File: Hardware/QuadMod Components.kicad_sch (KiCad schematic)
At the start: 119 parts, among them J1 Conn_01x08_Pin, J2 Conn_01x08_Pin, J3 Conn_01x08_Pin, J4 Conn_01x08_Pin, J5 Eurorack_10_pin_power, J7 Prog_Header, J7 USB_B_Micro, J8 Extra_Outs, U1 STF202-22T1G, U2 STM32H563VIT, U3 TL072, U4 MCP6004, U6 TPS561201, U7 LD1117-3.3-4Tab, U7 MCP6002-xSN, U9 AK4619VN, Y1 8MHz 20pF

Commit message: Clean up of schematics and PCBS
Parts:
- added J9: Test_Outs, Connector_PinHeader_2.54mm:PinHeader_1x02_P2.54mm_Vertical, symbol Connector:Conn_01x02_Pin
- added TP9: TestPoint, Custom_Footprints:1mm_Test_Point, symbol Connector:TestPoint
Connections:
- net +3.3VA: now also J4.4 (Pin_4); no longer J4.3 (Pin_3)
- net DLY_MIX: now also J4.3 (Pin_3); no longer J4.2 (Pin_2)
- net FX_MIX: now also J4.5 (Pin_5); no longer J4.4 (Pin_4)
- net GND: now also J4.1 (Pin_1), TP9.1; no longer J4.7 (Pin_7)
- net LFO_RANGE: now also J4.2 (Pin_2); no longer J4.1 (Pin_1)
- net OUT_AMP1: now also J4.7 (Pin_7); no longer J4.6 (Pin_6)
- net OUT_AMP2: now also J4.6 (Pin_6); no longer J4.5 (Pin_5)
- net Test_Out1: now reaches U2.78 (PC10)
- net Test_Out1: now also J9.1 (Pin_1)
- net Test_Out2: now reaches U2.79 (PC11)
- net Test_Out2: now also J9.2 (Pin_2)
- no-connect marks 50 -> 49
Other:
- note added: "(-5*-47/75) + (cv*-47/91) + (pot*-47/47) Pot=0 CV=0: 3.13V Pot=0 CV=6: 0.034V Pot=3.3 CV=0: -0.17V Pot=3.3 CV=5: -2.75V"
- note added: "Audio Codec"
- note added: "Av = -R_{FB} / R_{IN} Input: +7V, Output: (-12 * -14k/100k) + (+7 * -14k/68k) = 0.24V Input: -7V Output: (-12 * -14k/100k) + (-7 * -14k/68k) = 3.12V"
- note added: "Connectors"
- note added: "DAC Output is 2.83V_{PP} 10k/14k gives gain of 2.4 * 2.83 = 6.8V HPF Cutoff = 0.41Hz"
- note added: "MCU"
- note added: "USB"
- note removed: "Audio DAC"
- note removed: "Av = -R_{FB} / R_{IN} Input: +7V, Output: (-12 * -14k/100k) + (+7 * 14k/68k) = 0.24V Input: -7V Output: (-12 * -14k/100k) + (-7 * 14k/68k) = 3.12V"
- note removed: "DAC Output is 2.83V_{PP} 10k/14k gives gain of 2.4 * 2.83 = 6.8V"
- note removed: "POT Full scale: 3.3V CV Full scale: 6.4V"
- company: (none) -> Mountjoy Modular
- title: (none) -> QuadMod Components
- moved on the sheet: C12, C13, C18, C19, C38, C39, C40, C41, C42, C43, C44, D1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

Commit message: Draft Gerber Creation
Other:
- moved on the sheet: R10, R11, R12, R13, R14, R15, R16, R17, R6, R7, R8, R9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

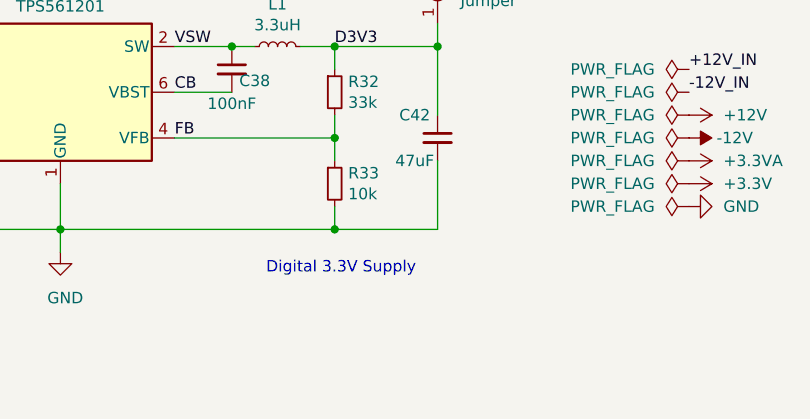
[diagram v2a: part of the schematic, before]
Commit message: Updated Production Gerbers; attempts to get USB working with O1 optimisation
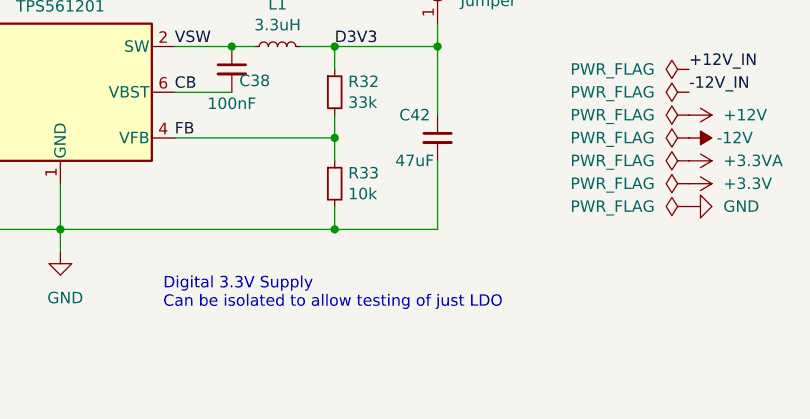
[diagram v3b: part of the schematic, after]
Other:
- note added: "Digital 3.3V Supply Can be isolated to allow testing of just LDO"
- note removed: "Digital 3.3V Supply"
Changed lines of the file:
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@@
     (effects (font (size 3 3) (thickness 0.6) bold) (justify left bottom))
   )
-  (text "Digital 3.3V Supply" (at 125.73 270.51 0)
+  (text "Digital 3.3V Supply\nCan be isolated to allow testing of just LDO"
+    (at 114.3 274.32 0)
     (effects (font (size 1.27 1.27)) (justify left bottom))
   )

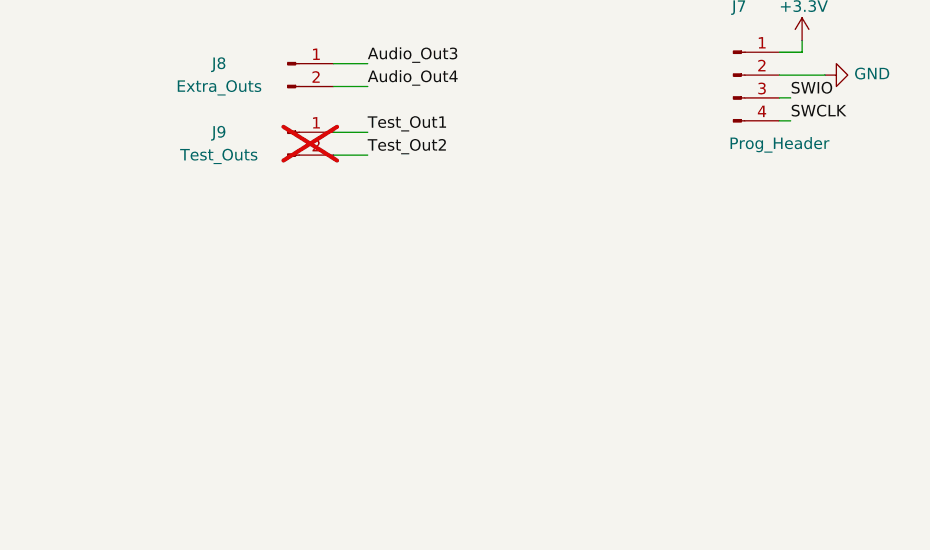
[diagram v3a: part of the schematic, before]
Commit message: Audio codec output tested and working
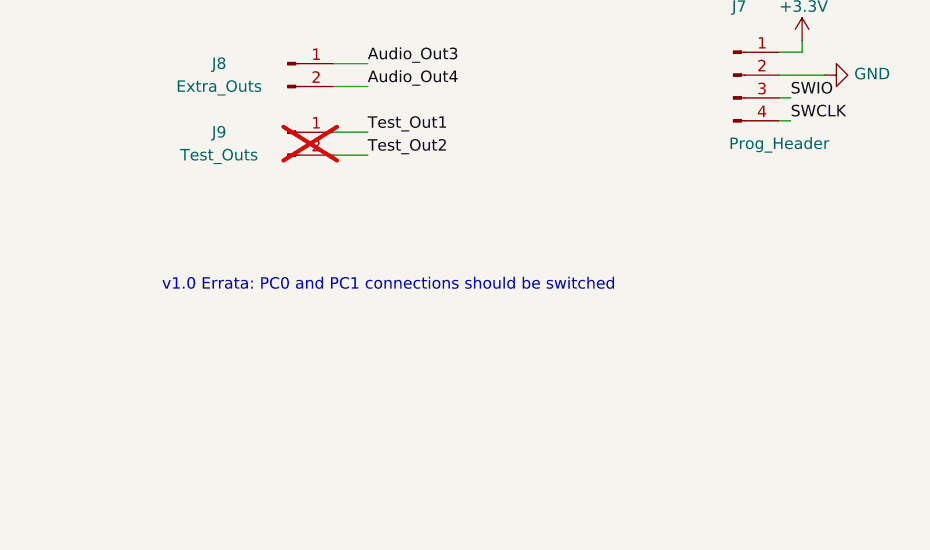
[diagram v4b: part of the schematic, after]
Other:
- note added: "v1.0 Errata: PC0 and PC1 connections should be switched"
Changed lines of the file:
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@@
+    (effects (font (size 1.27 1.27)) (justify left bottom))
+  )
+  (text "v1.0 Errata: PC0 and PC1 connections should be switched"
+    (at 303.53 257.81 0)
     (effects (font (size 1.27 1.27)) (justify left bottom))
   )

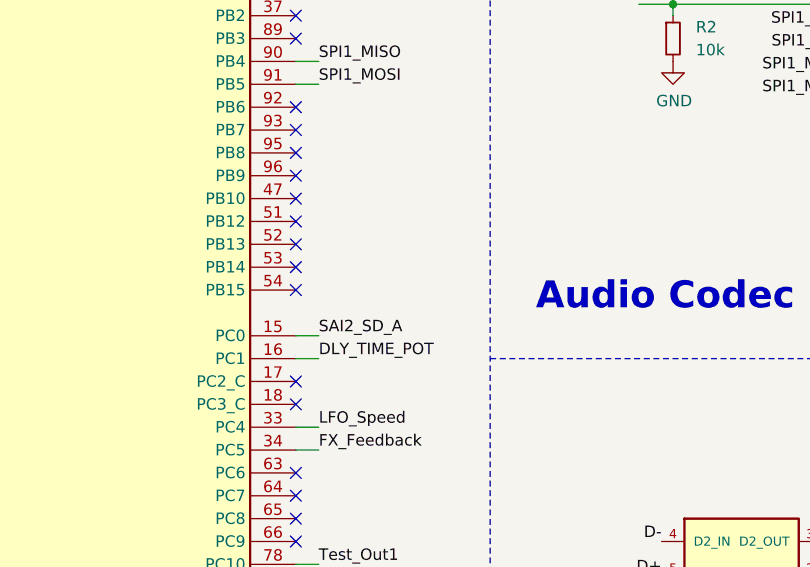
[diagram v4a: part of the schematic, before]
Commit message: Updated GpioPIn.h; basic delay LED working
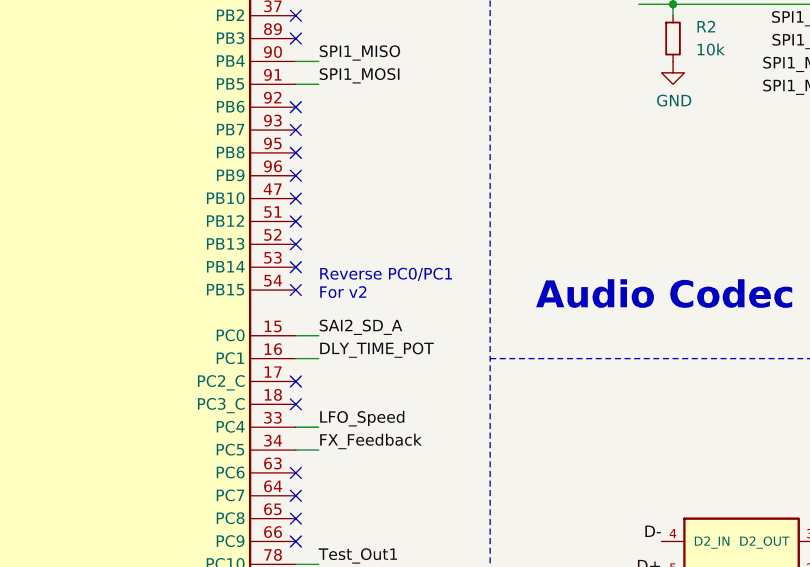
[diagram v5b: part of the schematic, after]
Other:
- note added: "Reverse PC0/PC1 For v2"
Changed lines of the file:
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@@
     (effects (font (size 1.27 1.27)) (justify left bottom))
+  )
+  (text "Reverse PC0/PC1 \nFor v2" (at 85.09 128.27 0)
+    (effects (font (size 1.27 1.27) (color 255 0 0 1)) (justify left bottom))
   )
   (text "USB" (at 109.22 189.23 0)
@@
   )
   (label "DLY_TIME_POT" (at 85.09 134.62 0) (fields_autoplaced)
-    (effects (font (size 1.27 1.27)) (justify left bottom))
+    (effects (font (size 1.27 1.27) (color 255 0 0 1)) (justify left bottom))
   )
   (label "SPI1_SCK" (at 85.09 60.96 0) (fields_autoplaced)
@@
   )
   (label "SAI2_SD_A" (at 85.09 132.08 0) (fields_autoplaced)
-    (effects (font (size 1.27 1.27)) (justify left bottom))
+    (effects (font (size 1.27 1.27) (color 255 0 0 1)) (justify left bottom))
   )
   (label "LFO_SPEED_POT" (at 250.19 217.17 0) (fields_autoplaced)

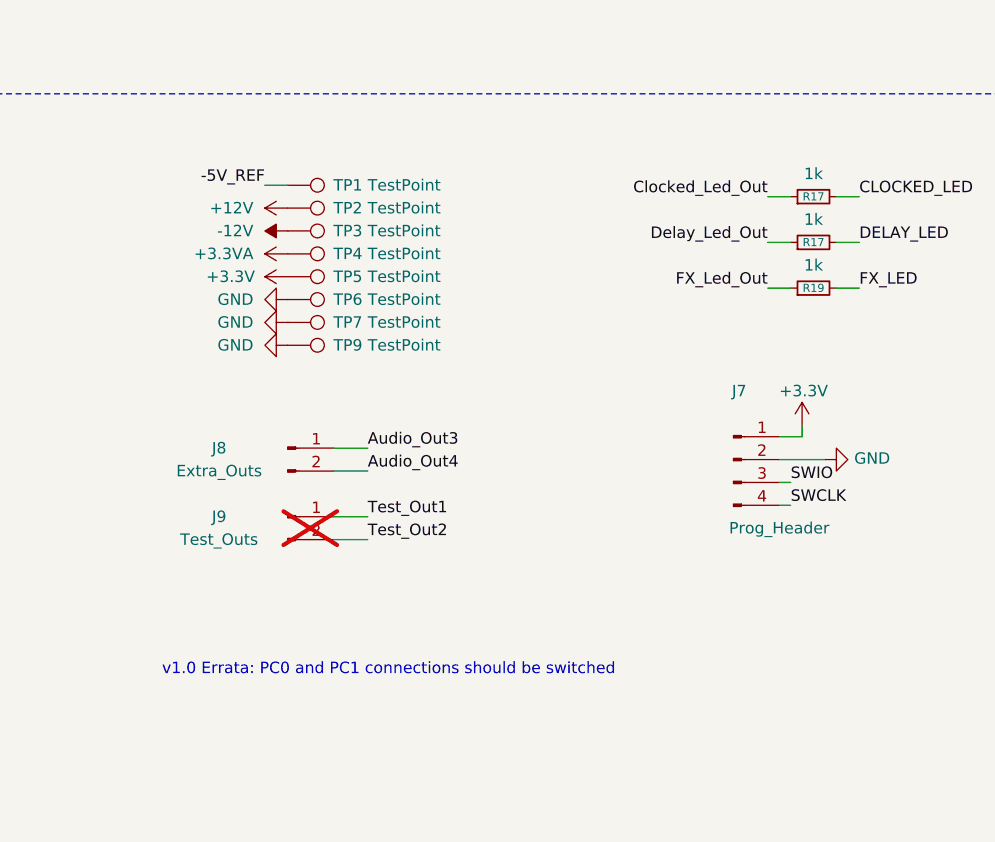
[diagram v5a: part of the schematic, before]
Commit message: Implemented effect switching
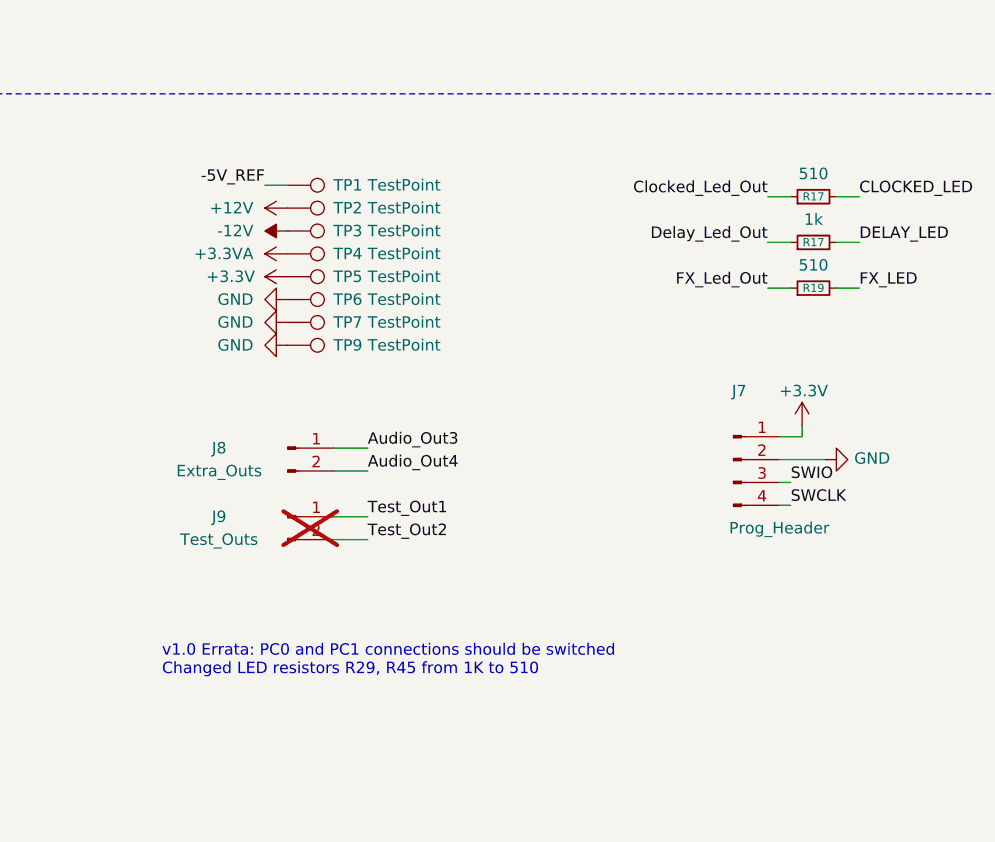
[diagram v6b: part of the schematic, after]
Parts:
- R17, R19: value 1k -> 510
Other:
- note added: "v1.0 Errata: PC0 and PC1 connections should be switched Changed LED resistors R29, R45 from 1K to 510"
- note removed: "v1.0 Errata: PC0 and PC1 connections should be switched"
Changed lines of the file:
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@@
     (effects (font (size 1.27 1.27)) (justify left bottom))
   )
-  (text "v1.0 Errata: PC0 and PC1 connections should be switched"
+  (text "v1.0 Errata: PC0 and PC1 connections should be switched\nChanged LED resistors R29, R45 from 1K to 510"
     (at 303.53 257.81 0)
     (effects (font (size 1.27 1.27)) (justify left bottom))
@@
       (effects (font (size 0.9 0.9)))
     )
-    (property "Value" "1k" (at 375.92 201.93 90)
+    (property "Value" "510" (at 375.92 201.93 90)
       (effects (font (size 1.27 1.27)))
     )
@@
       (effects (font (size 0.9 0.9)))
     )
-    (property "Value" "1k" (at 375.92 212.09 90)
+    (property "Value" "510" (at 375.92 212.09 90)
       (effects (font (size 1.27 1.27)))
     )
